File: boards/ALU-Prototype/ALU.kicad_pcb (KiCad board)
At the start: 2 copper layers, 67.9 x 99.1 mm, 118 parts

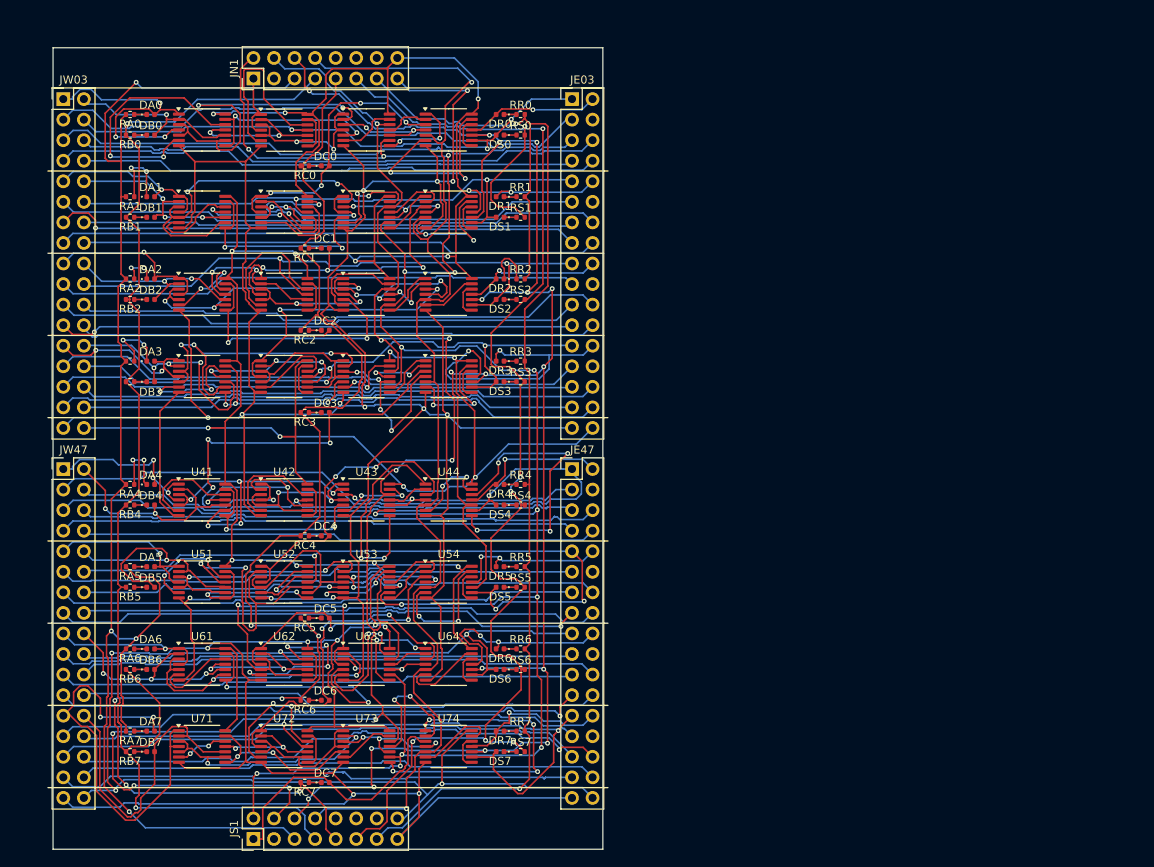
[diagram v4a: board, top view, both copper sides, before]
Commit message: Attempt to design the 8-bit ALU PCB
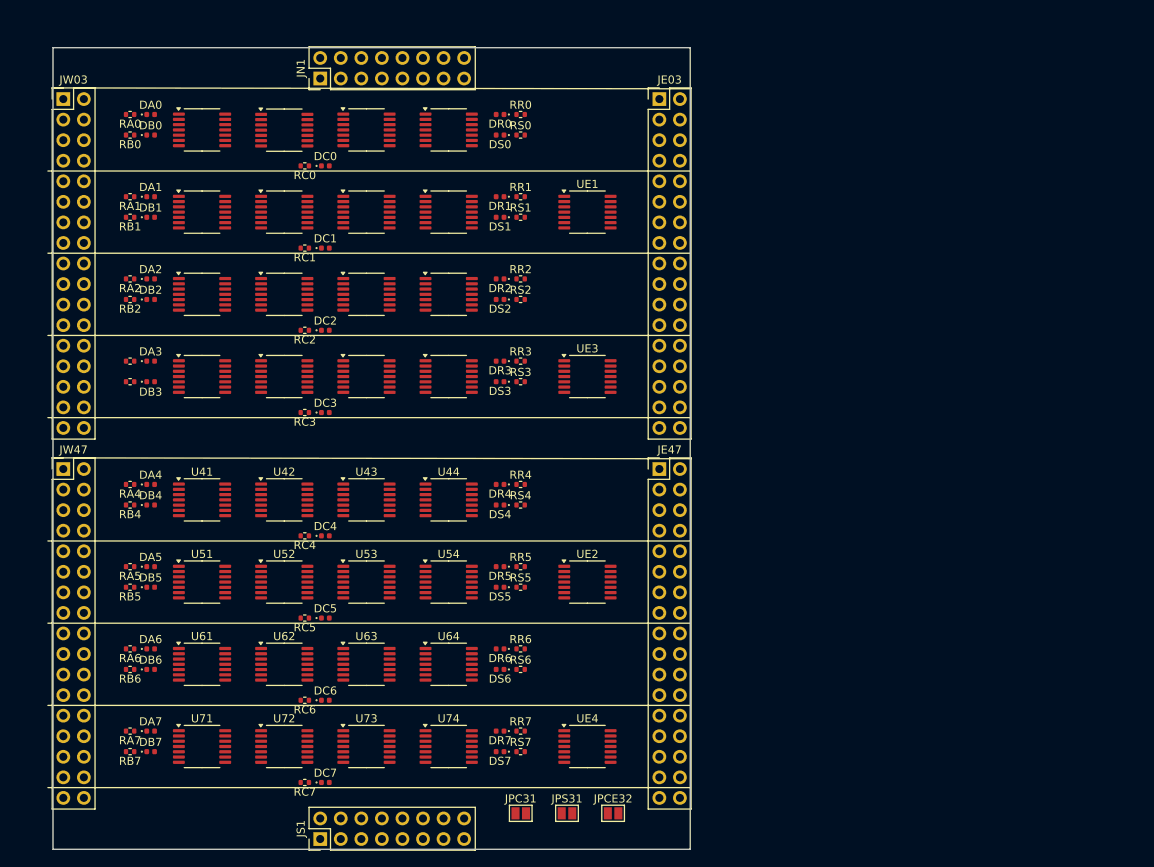
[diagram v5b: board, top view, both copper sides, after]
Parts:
- added JPC31: SolderJumper_2_Open, Jumper:SolderJumper-2_P1.3mm_Open_Pad1.0x1.5mm, F.Cu at (75.6, 112.4)
- added JPCE32: SolderJumper_2_Open, Jumper:SolderJumper-2_P1.3mm_Open_Pad1.0x1.5mm, F.Cu at (87.0, 112.4)
- added JPS31: SolderJumper_2_Open, Jumper:SolderJumper-2_P1.3mm_Open_Pad1.0x1.5mm, F.Cu at (81.3, 112.4)
- added UE1: ~, Package_SO:TSSOP-14_4.4x5mm_P0.65mm, F.Cu at (83.8, 38.1)
- added UE2: ~, Package_SO:TSSOP-14_4.4x5mm_P0.65mm, F.Cu at (83.8, 83.8)
- added UE3: ~, Package_SO:TSSOP-14_4.4x5mm_P0.65mm, F.Cu at (83.8, 58.4)
- added UE4: ~, Package_SO:TSSOP-14_4.4x5mm_P0.65mm, F.Cu at (83.8, 104.1)
- moved JE03 10.8 mm to (92.7, 24.1)
- moved JE47 10.8 mm to (92.7, 69.9)
- moved JN1 8.25 mm to (50.8, 21.6)
- moved JS1 8.25 mm to (50.8, 115.6)
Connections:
- net Net-(U02-Pad13) renamed E0
- net Net-(U12-Pad13) renamed E1
- net Net-(U22-Pad13) renamed E2
- net Net-(U32-Pad13) renamed E3
- net Net-(U42-Pad13) renamed E4
- net Net-(U52-Pad13) renamed E5
- net Net-(U62-Pad13) renamed E6
- net Net-(U72-Pad13) renamed E7
- JN1 pad 10: unconnected-(JN1-Pin_10-Pad10) -> S31
- JN1 pad 12: unconnected-(JN1-Pin_12-Pad12) -> C31
- JN1 pad 3: unconnected-(JN1-Pin_3-Pad3) -> E
- JS1 pad 10: unconnected-(JS1-Pin_10-Pad10) -> S31
- JS1 pad 12: unconnected-(JS1-Pin_12-Pad12) -> C31
- JS1 pad 3: unconnected-(JS1-Pin_3-Pad3) -> Ein
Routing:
- net VDD: track 536.9 -> 0.00 mm, vias 25 -> 0
- net GND: track 518.3 -> 0.00 mm, vias 15 -> 0
- net ADD: track 253.3 -> 0.00 mm, vias 15 -> 0
- net XOR: track 230.5 -> 0.00 mm, vias 17 -> 0
- net SUB: track 213.2 -> 0.00 mm, vias 9 -> 0
- net GNDC: track 179.1 -> 0.00 mm, vias 6 -> 0
- net GNDA: track 175.7 -> 0.00 mm, vias 4 -> 0
- net GNDS: track 166.7 -> 0.00 mm, vias 7 -> 0
- net GNDB: track 158.0 -> 0.00 mm, vias 2 -> 0
- net AND: track 152.3 -> 0.00 mm, vias 2 -> 0
- net GNDR: track 151.0 -> 0.00 mm, vias 2 -> 0
- net S5: track 89.3 -> 0.00 mm, vias 3 -> 0
- net S7: track 86.3 -> 0.00 mm, vias 2 -> 0
- net S4: track 85.5 -> 0.00 mm, vias 2 -> 0
- net S2: track 77.2 -> 0.00 mm, vias 2 -> 0
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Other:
- board size 67.9 x 99.1 mm -> 78.7 x 99.1 mm

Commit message: Routed PCB. BUT SetBit0 is missing !
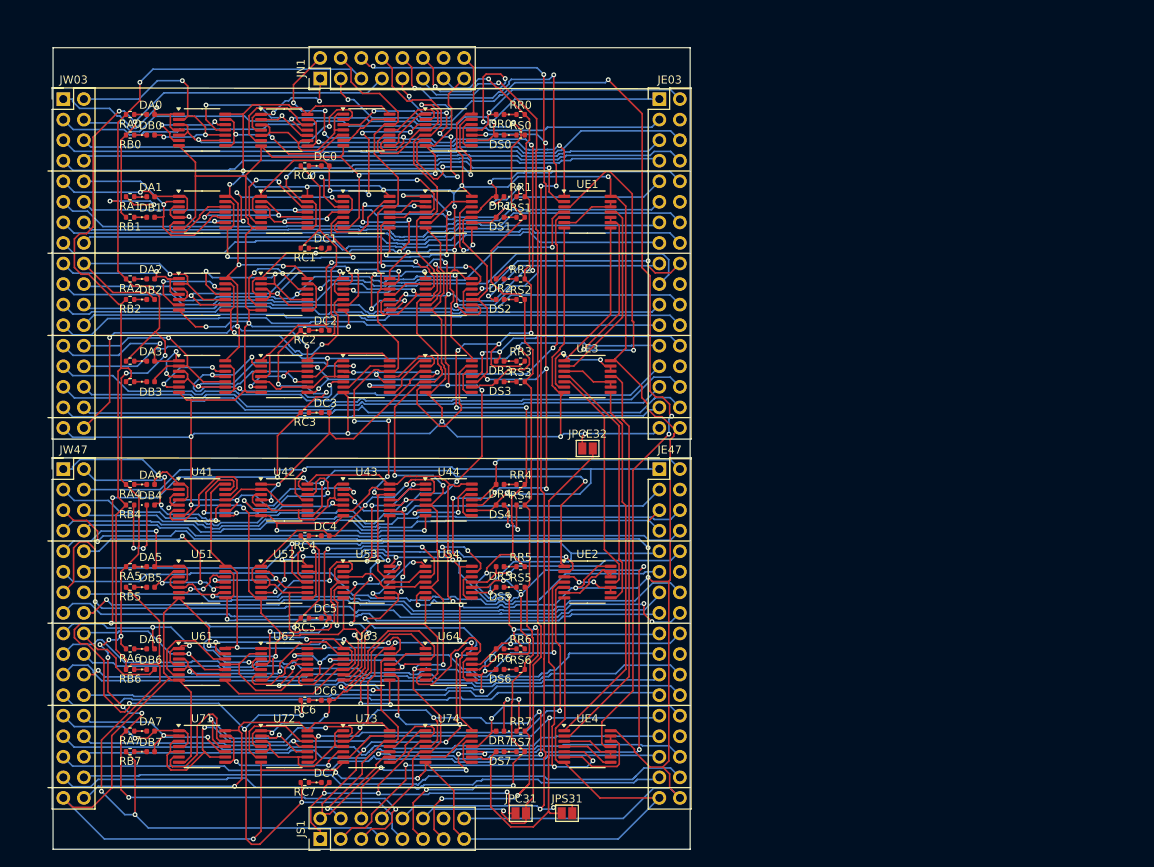
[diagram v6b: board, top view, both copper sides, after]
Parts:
- moved JPCE32 45.2 mm to (83.8, 67.3)
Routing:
- net GND: track 0.00 -> 597.2 mm, vias 0 -> 19
- net VDD: track 0.00 -> 572.7 mm, vias 0 -> 26
- net XOR: track 0.00 -> 260.3 mm, vias 0 -> 18
- net GNDC: track 0.00 -> 254.9 mm, vias 0 -> 16
- net ADD: track 0.00 -> 246.3 mm, vias 0 -> 23
- net GNDB: track 0.00 -> 207.9 mm, vias 0 -> 4
- net GNDA: track 0.00 -> 191.6 mm, vias 0 -> 13
- net GNDR: track 0.00 -> 163.9 mm, vias 0 -> 12
- net SUB: track 0.00 -> 139.9 mm, vias 0 -> 11
- net S31: track 0.00 -> 139.8 mm, vias 0 -> 6
- net GNDS: track 0.00 -> 136.9 mm, vias 0 -> 5
- net AND: track 0.00 -> 130.3 mm, vias 0 -> 4
- net E: track 0.00 -> 129.2 mm, vias 0 -> 4
- net C31: track 0.00 -> 122.3 mm, vias 0 -> 3
- net S7: track 0.00 -> 106.9 mm, vias 0 -> 2
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
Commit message: SetBit0 and routing of the PCB
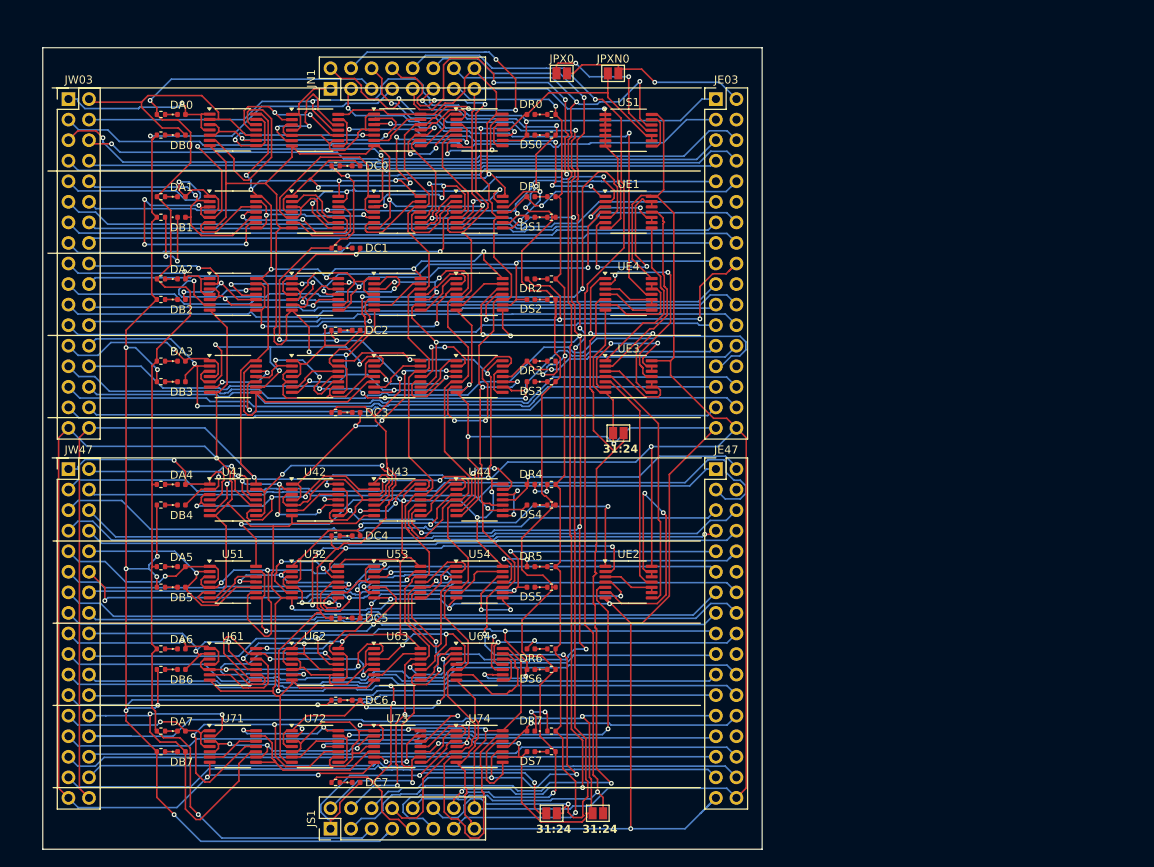
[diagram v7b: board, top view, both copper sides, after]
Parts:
- added JPX0: ~, Jumper:SolderJumper-2_P1.3mm_Open_Pad1.0x1.5mm, F.Cu at (80.6, 21.0)
- added JPXN0: ~, Jumper:SolderJumper-2_P1.3mm_Open_Pad1.0x1.5mm, F.Cu at (87.0, 21.0)
- added US1: ~, Package_SO:TSSOP-14_4.4x5mm_P0.65mm, F.Cu at (88.9, 28.0)
- JPC31, JPS31: value SolderJumper_2_Open -> ~
- JPE32: renamed from JPCE32; value SolderJumper_2_Open -> ~
- moved UE4 56.1 mm to (88.9, 48.3)
- moved JE03 6.98 mm to (99.7, 24.1)
- moved JE47 6.98 mm to (99.7, 69.9)
- moved UE1 5.08 mm to (88.9, 38.1)
- moved UE2 5.08 mm to (88.9, 83.8)
- moved UE3 5.08 mm to (88.9, 58.4)
- moved JPE32 4.26 mm to (87.6, 65.4)
- moved DA4 3.81 mm to (33.7, 71.8)
- moved DA5 3.81 mm to (33.7, 81.9)
- moved DA6 3.81 mm to (33.7, 92.1)
- moved DA7 3.81 mm to (33.7, 102.2)
- moved DB4 3.81 mm to (33.7, 74.3)
- moved DB5 3.81 mm to (33.7, 84.5)
- moved DB6 3.81 mm to (33.7, 94.6)
- moved DB7 3.81 mm to (33.7, 104.8)
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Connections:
- DR0 pad 2: R0 -> /ALUSlice0/R
- JN1 pad 14: unconnected-(JN1-Pin_14-Pad14) -> !SET0
- JS1 pad 14: unconnected-(JS1-Pin_14-Pad14) -> !SET0
- U04 pad 11: R0 -> /ALUSlice0/R
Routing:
- net !SET0: track 0.00 -> 137.4 mm, vias 0 -> 4
- net VDD: track 572.7 -> 661.7 mm, vias 26 -> 25
- net XOR: track 260.3 -> 172.9 mm, vias 18 -> 10
- net E: track 129.2 -> 60.5 mm, vias 4 -> 2
- net GND: track 597.2 -> 659.7 mm, vias 19 -> 18
- net Net-(UE1-Pad10): track 56.2 -> 11.8 mm
- net Net-(U11-Pad3): track 30.2 -> 73.0 mm, vias 5 -> 6
- net S7: track 106.9 -> 144.3 mm, vias 2 -> 3
- net GNDR: track 163.9 -> 128.5 mm, vias 12 -> 4
- net GNDA: track 191.6 -> 157.2 mm, vias 13 -> 2
- net Net-(U73-Pad10): track 59.3 -> 29.1 mm, vias 5 -> 4
- net GNDC: track 254.9 -> 225.7 mm, vias 16 -> 11
- net GNDB: track 207.9 -> 180.4 mm, vias 4 -> 9
- net /ALUSlice0/R: track 0.00 -> 25.9 mm
- net Net-(UE2-Pad12): track 8.17 -> 33.4 mm, vias 0 -> 2
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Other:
- board size 78.7 x 99.1 mm -> 88.9 x 99.1 mm
- board text added: "31:24"

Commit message: Mounting holes. PCB title.
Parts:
- added REF**: MountingHole_3mm, MountingHole:MountingHole_3mm, F.Cu at (95.3, 21.0)
- added REF**: MountingHole_3mm, MountingHole:MountingHole_3mm, F.Cu at (27.9, 113.7)
- added REF**: MountingHole_3mm, MountingHole:MountingHole_3mm, F.Cu at (94.6, 113.7)
- added REF**: MountingHole_3mm, MountingHole:MountingHole_3mm, F.Cu at (27.3, 21.0)
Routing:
- net GND: track 659.7 -> 654.5 mm, vias 18 -> 19
- net S7: track 144.3 -> 139.1 mm
- net R0: track 24.0 -> 27.6 mm
- net XOR: track 172.9 -> 170.7 mm
- net SUB: track 163.2 -> 161.2 mm
- net Ein: track 103.8 -> 102.6 mm
- net PD2: track 82.7 -> 81.6 mm
- net PD1: track 83.8 -> 82.9 mm
- net PA0: track 84.4 -> 83.5 mm
- net PB6: track 83.2 -> 82.5 mm
- net PA6: track 84.7 -> 84.1 mm
- net PD4: track 83.7 -> 83.1 mm
- net GNDB: track 180.4 -> 179.8 mm
- net PD6: track 83.7 -> 83.2 mm
- net PE4: track 82.1 -> 81.6 mm
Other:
- board text added: "31:8"
- board text added: "7:0"
- board text added: "RV74-ALU-P2"
